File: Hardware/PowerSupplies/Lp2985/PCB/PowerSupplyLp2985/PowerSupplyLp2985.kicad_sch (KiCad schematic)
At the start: 6 parts, among them J1 Conn_01x02_Pin, J2 Barrel_Jack, U1 LM7805_TO220

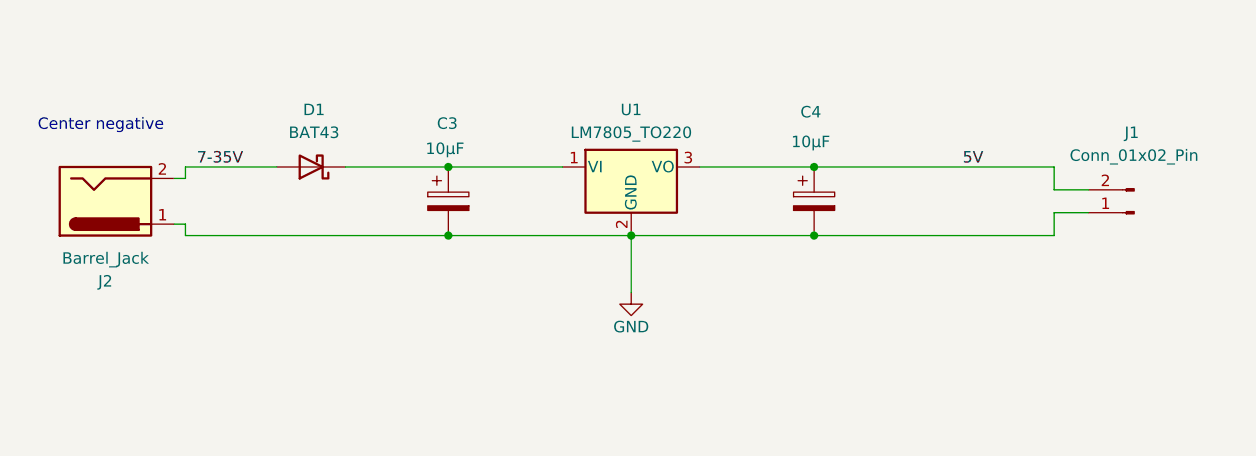
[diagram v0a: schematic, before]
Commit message: power supplies added
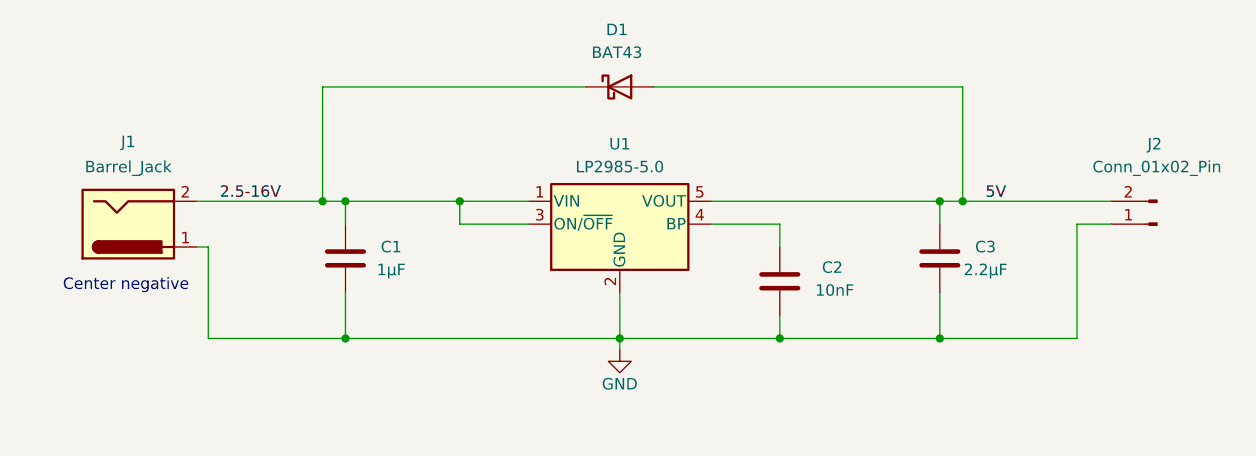
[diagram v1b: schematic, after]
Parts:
- removed C3, C4: 10μF, Capacitor_THT:C_Radial_D6.3mm_H7.0mm_P2.50mm, symbol Device:C_Polarized
- removed J1: Conn_01x02_Pin, Connector_PinSocket_2.54mm:PinSocket_1x02_P2.54mm_Horizontal, symbol Connector:Conn_01x02_Pin
- removed J2: Barrel_Jack, Connector_BarrelJack:BarrelJack_GCT_DCJ200-10-A_Horizontal, symbol Connector:Barrel_Jack
- removed U1: LM7805_TO220, Package_TO_SOT_THT:TO-220-3_Vertical, symbol Regulator_Linear:LM7805_TO220
- added C1: 1μF, Capacitor_THT:C_Disc_D5.0mm_W2.5mm_P5.00mm, symbol Device:C
- added C2: 10nF, Capacitor_THT:C_Disc_D5.0mm_W2.5mm_P2.50mm, symbol Device:C
- added C3: 2.2μF, Capacitor_THT:C_Disc_D5.0mm_W2.5mm_P5.00mm, symbol Device:C
- added J1: Barrel_Jack, Connector_BarrelJack:BarrelJack_GCT_DCJ200-10-A_Horizontal, symbol Connector:Barrel_Jack
- added J2: Conn_01x02_Pin, Connector_PinSocket_2.54mm:PinSocket_1x02_P2.54mm_Horizontal, symbol Connector:Conn_01x02_Pin
- added U1: LP2985-5.0, Package_TO_SOT_SMD:SOT-23-5, symbol Regulator_Linear:LP2985-5.0
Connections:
- net 7-35V is gone; now on net 5V: D1.2 (A)
- net 5V: now also C3.1, J2.2 (Pin_2), U1.5 (VOUT)
- net GND: now also C1.2, C2.1, C3.2, J1.1, J2.1 (Pin_1), U1.2 (GND)
- net 2.5-16V: now reaches D1.1 (K)
- net 2.5-16V: now also C1.1, J1.2, U1.1 (VIN), U1.3 (ON/~{OFF})
- new net: C2.2, U1.4 (BP)
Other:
- title: Daisy Seed Development Kit Power Supply LM7805 -> (none)

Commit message: Added consistency
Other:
- note added: "All capacitors are ceramic"
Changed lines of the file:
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@@
+		)
+	)
+	(text "All capacitors are ceramic"
+		(exclude_from_sim no)
+		(at 143.51 111.506 0)
+		(effects
+			(font
+				(size 1.27 1.27)
+			)
 		)
 	)
